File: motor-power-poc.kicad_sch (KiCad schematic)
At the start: 59 parts, among them J4 USB_C_Receptacle_USB2.0_14P, SW1 SW_Push, SW2 SW_Push, U1 ESP32-S3FH4R2, U2 TPS5430DDA, U3 TPS2121, Y1 48M

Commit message: schem: update VBUS TVS diode
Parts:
- D3: value H5VU10U -> P6SMB6.8CA/TR13; footprint Pers:Diode_DFN1006 -> Diode_SMD:D_SMB; Basic E -> Y; JLCPCB Part # C22395519 -> C78395; Manufacturer hongjiacheng -> Brightking; Manufacturer Part Number H5VU10U -> P6SMB6.8CA/TR13
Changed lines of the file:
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@@
 			)
 		)
-		(property "Value" "H5VU10U"
+		(property "Value" "P6SMB6.8CA/TR13"
 			(at 54.61 142.2399 90)
 			(effects
@@
 			)
 		)
-		(property "Footprint" "Pers:Diode_DFN1006"
+		(property "Footprint" "Diode_SMD:D_SMB"
 			(at 61.595 140.97 0)
 			(effects
@@
 			)
 		)
-		(property "Datasheet" "https://datasheet.lcsc.com/lcsc/2504101957_hongjiacheng-H5VU10U_C22395519.pdf"
+		(property "Datasheet" "https://www.lcsc.com/datasheet/C78395.pdf"
 			(at 57.15 140.97 0)
 			(effects
@@
 			)
 		)
-		(property "Description" "-55℃~+155℃ 0.8pF 16V 200nA 55W@8/20us 5A@8/20us 5V 6V ESD IEC 61000-4-2 Unidirectional DFN1006-2L ESD and Surge Protection (TVS/ESD) ROHS"
+		(property "Description" "10.5V 1uA 5.8V 58.1A 6.45V 600W Bidirectional TVS SMB(DO-214AA) ESD and Surge Protection (TVS/ESD) ROHS"
 			(at 57.15 140.97 0)
 			(effects
@@
 			)
 		)
-		(property "Basic" "E"
+		(property "Basic" "Y"
 			(at 57.15 140.97 90)
 			(effects
@@
 			)
 		)
-		(property "JLCPCB Part #" "C22395519"
+		(property "JLCPCB Part #" "C78395"
 			(at 57.15 140.97 90)
 			(effects
@@
 			)
 		)
-		(property "Manufacturer" "hongjiacheng"
+		(property "Manufacturer" "Brightking"
 			(at 57.15 140.97 90)
 			(effects
@@
 			)
 		)
-		(property "Manufacturer Part Number" "H5VU10U"
+		(property "Manufacturer Part Number" "P6SMB6.8CA/TR13"
 			(at 57.15 140.97 90)
 			(effects

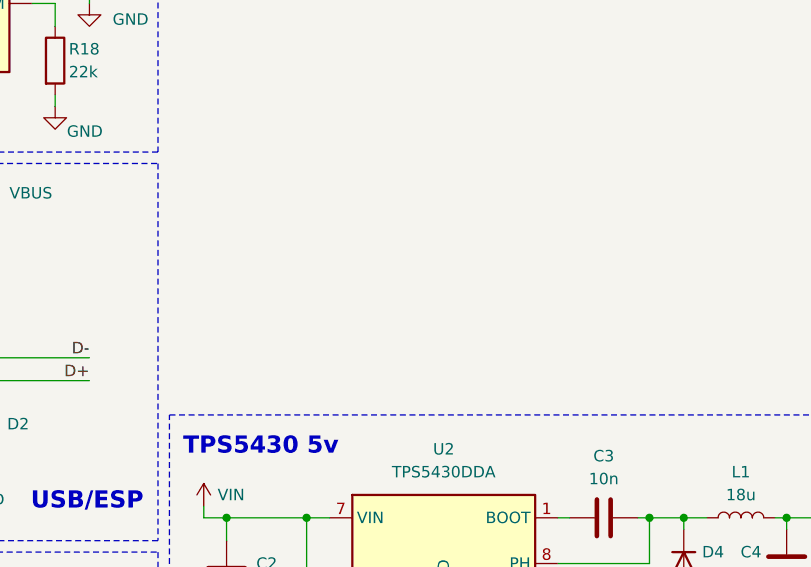
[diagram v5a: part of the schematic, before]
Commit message: schem: add LDL212 3V3 ldo
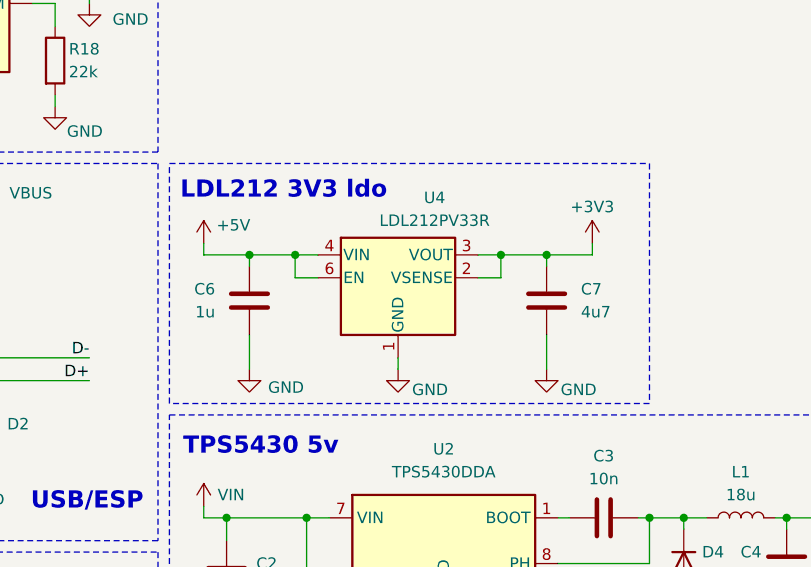
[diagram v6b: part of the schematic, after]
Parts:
- added C6: 1u, symbol Device:C
- added C7: 4u7, symbol Device:C
- added U4: LDL212PV33R, Pers:DFN-6-1EP_2x2mm_P0.5mm_ST, symbol Pers:LDL212PV33R
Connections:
- net +3V3: now also C7.1, U4.2 (VSENSE), U4.3 (VOUT)
- net +5V: now also C6.1, U4.4 (VIN), U4.6 (EN)
- net GND: now also C6.2, C7.2, U4.1 (GND)
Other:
- note added: "LDL212 3V3 ldo"

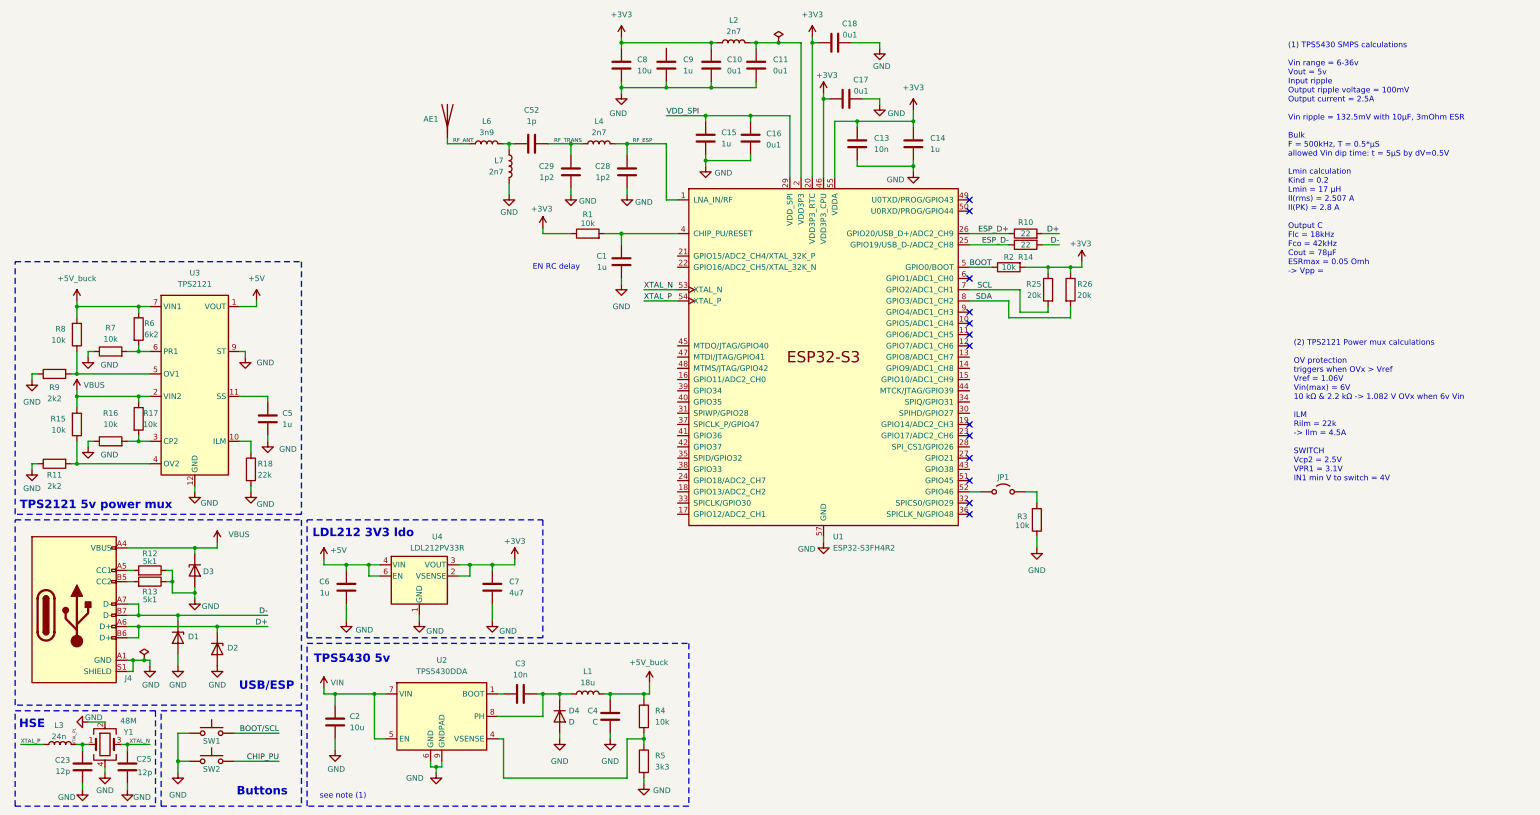
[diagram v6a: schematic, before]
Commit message: schem: moved connectors to separate sheet
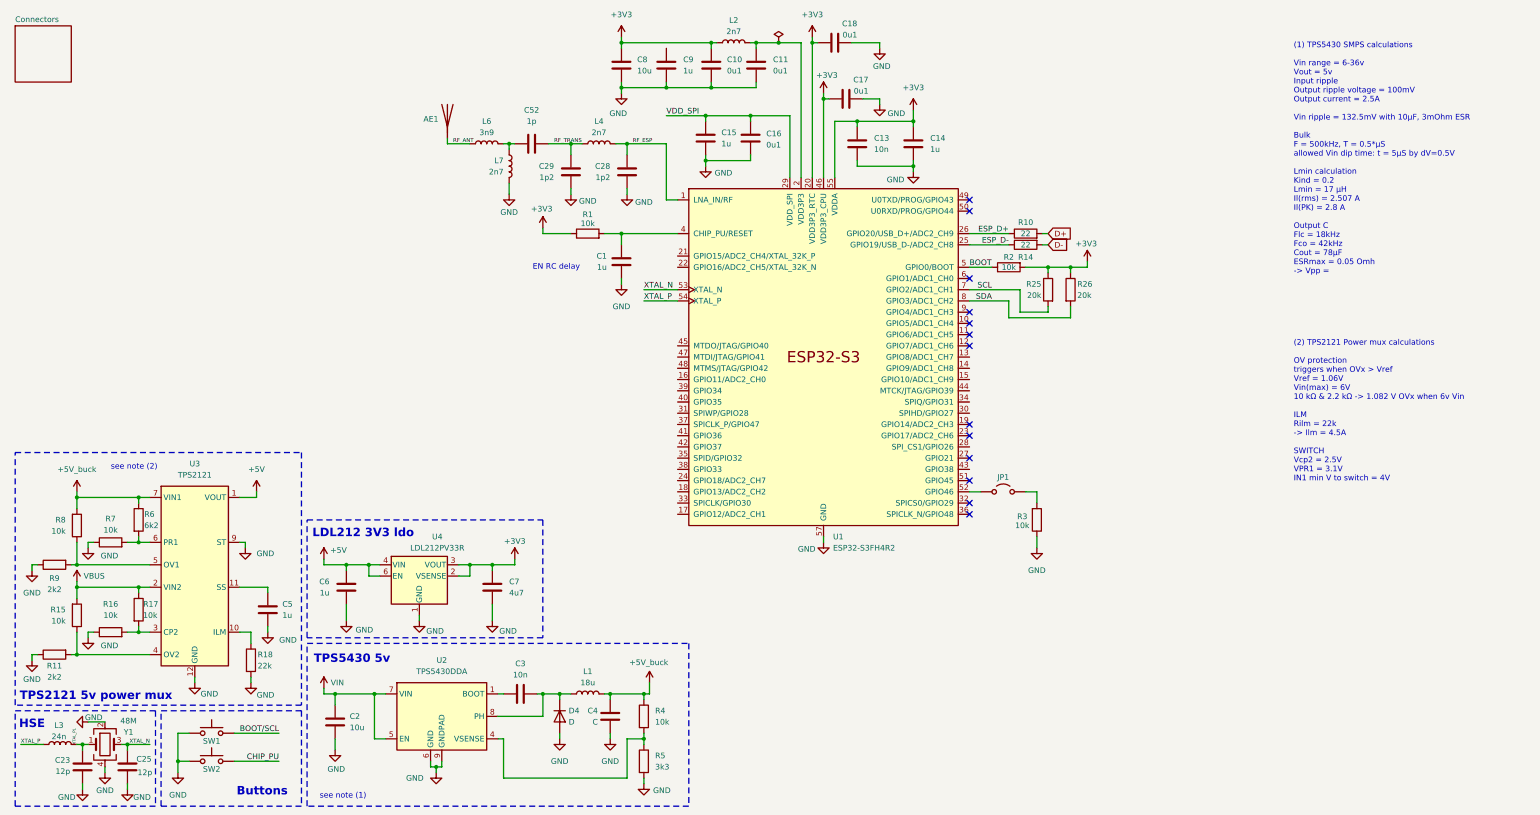
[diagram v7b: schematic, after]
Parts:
- removed D1, D2: H5VU10U, Pers:Diode_DFN1006, symbol Pers:H5VU10U
- removed D3: P6SMB6.8CA/TR13, Diode_SMD:D_SMB, symbol Pers:H5VU10U
- removed J4: USB_C_Receptacle_USB2.0_14P, Connector_USB:USB_C_Receptacle_HRO_TYPE-C-31-M-12, symbol Connector:USB_C_Receptacle_USB2.0_14P
- removed R12, R13: 5k1, Resistor_SMD:R_0402_1005Metric, symbol Device:R
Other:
- added sheet Connectors (connectors.kicad_sch)
- note added: "see note (2)"
- note removed: "USB/ESP"
- moved on the sheet: C5, R11, R15, R16, R17, R18, R6, R7, R8, R9, U3

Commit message: schem: moved ldo, smps and power mux to power sheet
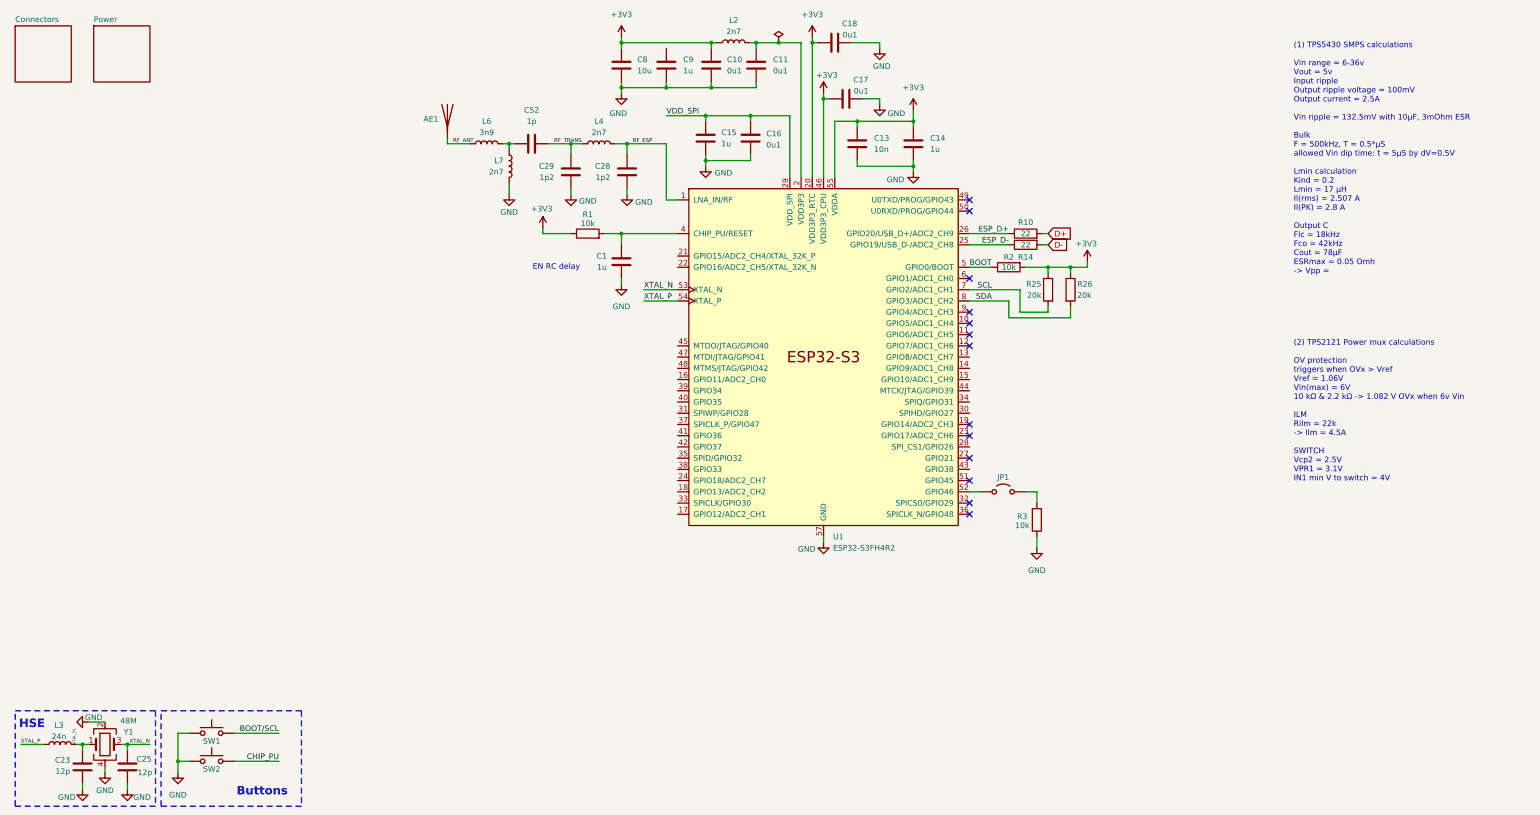
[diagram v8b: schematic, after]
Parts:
- removed C2: 10u, symbol Device:C
- removed C3: 10n, symbol Device:C
- removed C4: C, symbol Device:C
- removed C5, C6: 1u, symbol Device:C
- removed C7: 4u7, symbol Device:C
- removed D4: D, symbol Device:D
- removed L1: 18u, symbol Device:L
- removed R11, R9: 2k2, symbol Device:R
- removed R15, R16, R17, R4, R7, R8: 10k, symbol Device:R
- removed R18: 22k, symbol Device:R
- removed R5: 3k3, symbol Device:R
- removed R6: 6k2, symbol Device:R
- removed U2: TPS5430DDA, Package_SO:TI_SO-PowerPAD-8_ThermalVias, symbol Regulator_Switching:TPS5430DDA
- removed U3: TPS2121, Package_DFN_QFN:Texas_VQFN-HR-12_2x2.5mm_P0.5mm_ThermalVias, symbol Pers:TPS2121
- removed U4: LDL212PV33R, Pers:DFN-6-1EP_2x2mm_P0.5mm_ST, symbol Pers:LDL212PV33R
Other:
- added sheet Power (power.kicad_sch)
- note removed: "LDL212 3V3 ldo"
- note removed: "TPS2121 5v power mux"
- note removed: "TPS5430 5v"
- note removed: "see note (1)"
- note removed: "see note (2)"
